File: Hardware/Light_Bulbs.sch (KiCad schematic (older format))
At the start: 44 parts, among them J1 DNP, Q1 2N2222A, Q2 2N2222A, Q3 2N2222A, Q4 2N2222A, U1 PIC18F23K22

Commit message: Replaced light bulb through-hole resistors by SMD ones.
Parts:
- R92, R93, R94, R95: footprint Resistor_THT:R_Axial_DIN0207_L6.3mm_D2.5mm_P7.62mm_Horizontal -> Resistor_SMD:R_1206_3216Metric_Pad1.42x1.75mm_HandSolder
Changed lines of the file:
@@
 EESchema Schematic File Version 4
-LIBS:Chrismas_Tree-cache
 EELAYER 30 0
 EELAYER END
@@
 F 0 "R95" V 1407 5850 50  0000 C CNN
 F 1 "220" V 1316 5850 50  0000 C CNN
-F 2 "Resistor_THT:R_Axial_DIN0207_L6.3mm_D2.5mm_P7.62mm_Horizontal" V 1130 5850 50  0001 C CNN
+F 2 "Resistor_SMD:R_1206_3216Metric_Pad1.42x1.75mm_HandSolder" V 1130 5850 50  0001 C CNN
 F 3 "~" H 1200 5850 50  0001 C CNN
 	1    1200 5850
@@
 F 0 "R94" V 1407 6300 50  0000 C CNN
 F 1 "220" V 1316 6300 50  0000 C CNN
-F 2 "Resistor_THT:R_Axial_DIN0207_L6.3mm_D2.5mm_P7.62mm_Horizontal" V 1130 6300 50  0001 C CNN
+F 2 "Resistor_SMD:R_1206_3216Metric_Pad1.42x1.75mm_HandSolder" V 1130 6300 50  0001 C CNN
 F 3 "~" H 1200 6300 50  0001 C CNN
 	1    1200 6300
@@
 F 0 "R93" V 1407 6750 50  0000 C CNN
 F 1 "220" V 1316 6750 50  0000 C CNN
-F 2 "Resistor_THT:R_Axial_DIN0207_L6.3mm_D2.5mm_P7.62mm_Horizontal" V 1130 6750 50  0001 C CNN
+F 2 "Resistor_SMD:R_1206_3216Metric_Pad1.42x1.75mm_HandSolder" V 1130 6750 50  0001 C CNN
 F 3 "~" H 1200 6750 50  0001 C CNN
 	1    1200 6750
@@
 F 0 "R92" V 1407 7200 50  0000 C CNN
 F 1 "220" V 1316 7200 50  0000 C CNN
-F 2 "Resistor_THT:R_Axial_DIN0207_L6.3mm_D2.5mm_P7.62mm_Horizontal" V 1130 7200 50  0001 C CNN
+F 2 "Resistor_SMD:R_1206_3216Metric_Pad1.42x1.75mm_HandSolder" V 1130 7200 50  0001 C CNN
 F 3 "~" H 1200 7200 50  0001 C CNN
 	1    1200 7200

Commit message: Replaced though-hole capacitors by SMD ones.
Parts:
- C1, C2, C3, C4: footprint Capacitor_THT:C_Disc_D5.0mm_W2.5mm_P5.00mm -> Capacitor_SMD:C_1206_3216Metric_Pad1.42x1.75mm_HandSolder
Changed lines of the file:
@@
 F 0 "C4" H 8865 5646 50  0000 L CNN
 F 1 "100n-25V" H 8865 5555 50  0000 L CNN
-F 2 "Capacitor_THT:C_Disc_D5.0mm_W2.5mm_P5.00mm" H 8788 5450 50  0001 C CNN
+F 2 "Capacitor_SMD:C_1206_3216Metric_Pad1.42x1.75mm_HandSolder" H 8788 5450 50  0001 C CNN
 F 3 "~" H 8750 5600 50  0001 C CNN
 	1    8750 5600
@@
 F 0 "C1" H 4665 2746 50  0000 L CNN
 F 1 "100n-25V" H 4600 2600 50  0000 L CNN
-F 2 "Capacitor_THT:C_Disc_D5.0mm_W2.5mm_P5.00mm" H 4588 2550 50  0001 C CNN
+F 2 "Capacitor_SMD:C_1206_3216Metric_Pad1.42x1.75mm_HandSolder" H 4588 2550 50  0001 C CNN
 F 3 "~" H 4550 2700 50  0001 C CNN
 	1    4550 2700
@@
 F 0 "C2" H 5215 2746 50  0000 L CNN
 F 1 "1u-25V" H 5150 2600 50  0000 L CNN
-F 2 "Capacitor_THT:C_Disc_D5.0mm_W2.5mm_P5.00mm" H 5138 2550 50  0001 C CNN
+F 2 "Capacitor_SMD:C_1206_3216Metric_Pad1.42x1.75mm_HandSolder" H 5138 2550 50  0001 C CNN
 F 3 "~" H 5100 2700 50  0001 C CNN
 	1    5100 2700
@@
 F 0 "C3" H 5715 2746 50  0000 L CNN
 F 1 "10u-25V" H 5650 2600 50  0000 L CNN
-F 2 "Capacitor_THT:C_Disc_D5.0mm_W2.5mm_P5.00mm" H 5638 2550 50  0001 C CNN
+F 2 "Capacitor_SMD:C_1206_3216Metric_Pad1.42x1.75mm_HandSolder" H 5638 2550 50  0001 C CNN
 F 3 "~" H 5600 2700 50  0001 C CNN
 	1    5600 2700

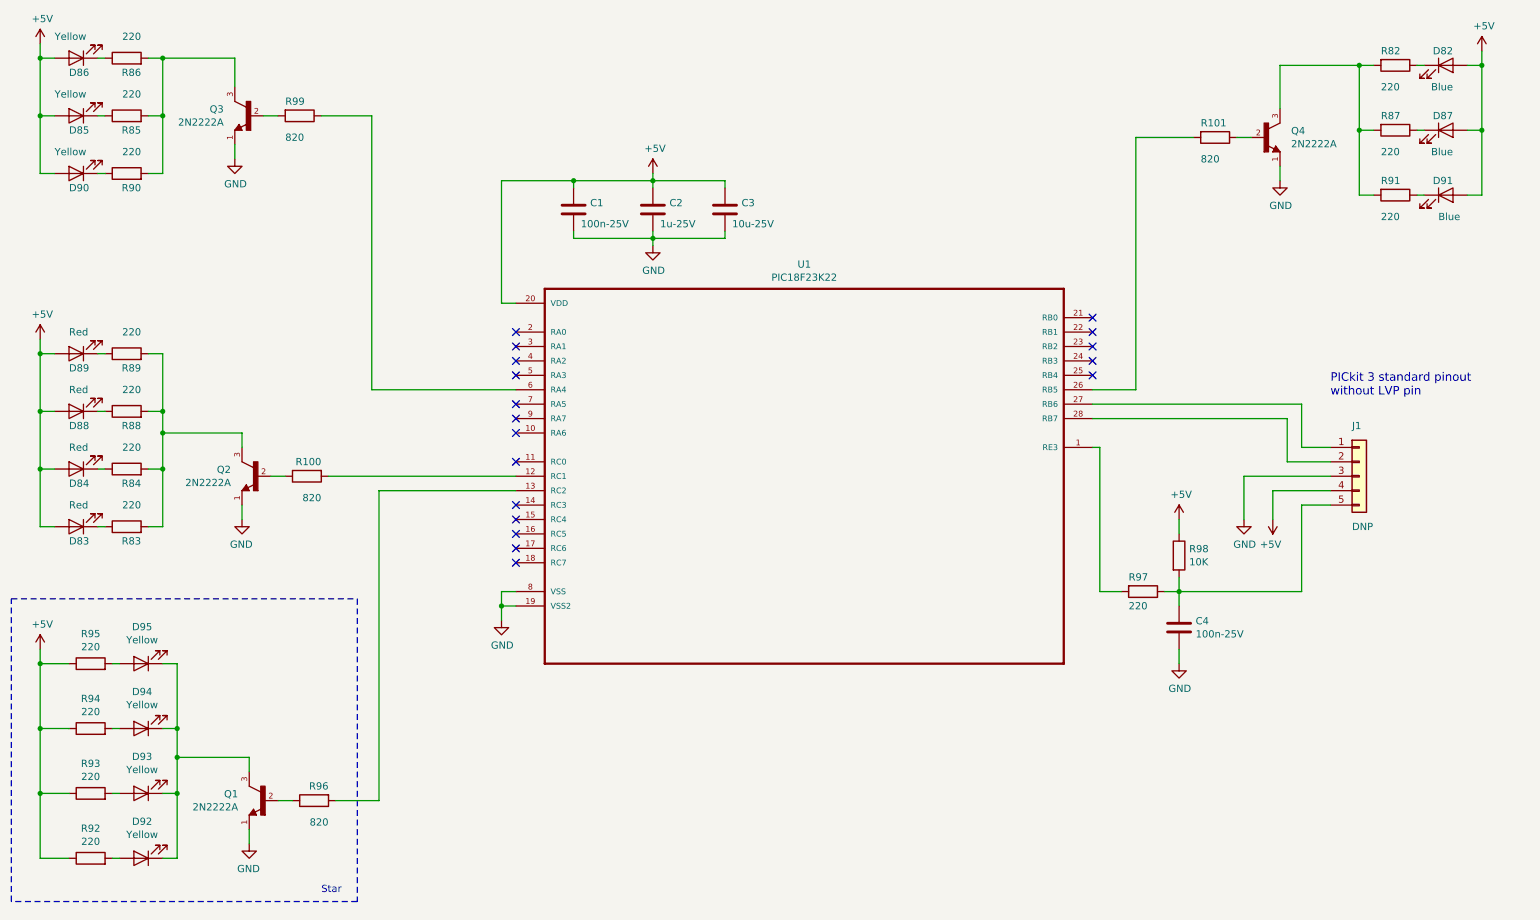
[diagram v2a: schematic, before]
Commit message: Replaced through-hole transistors by SMD ones.
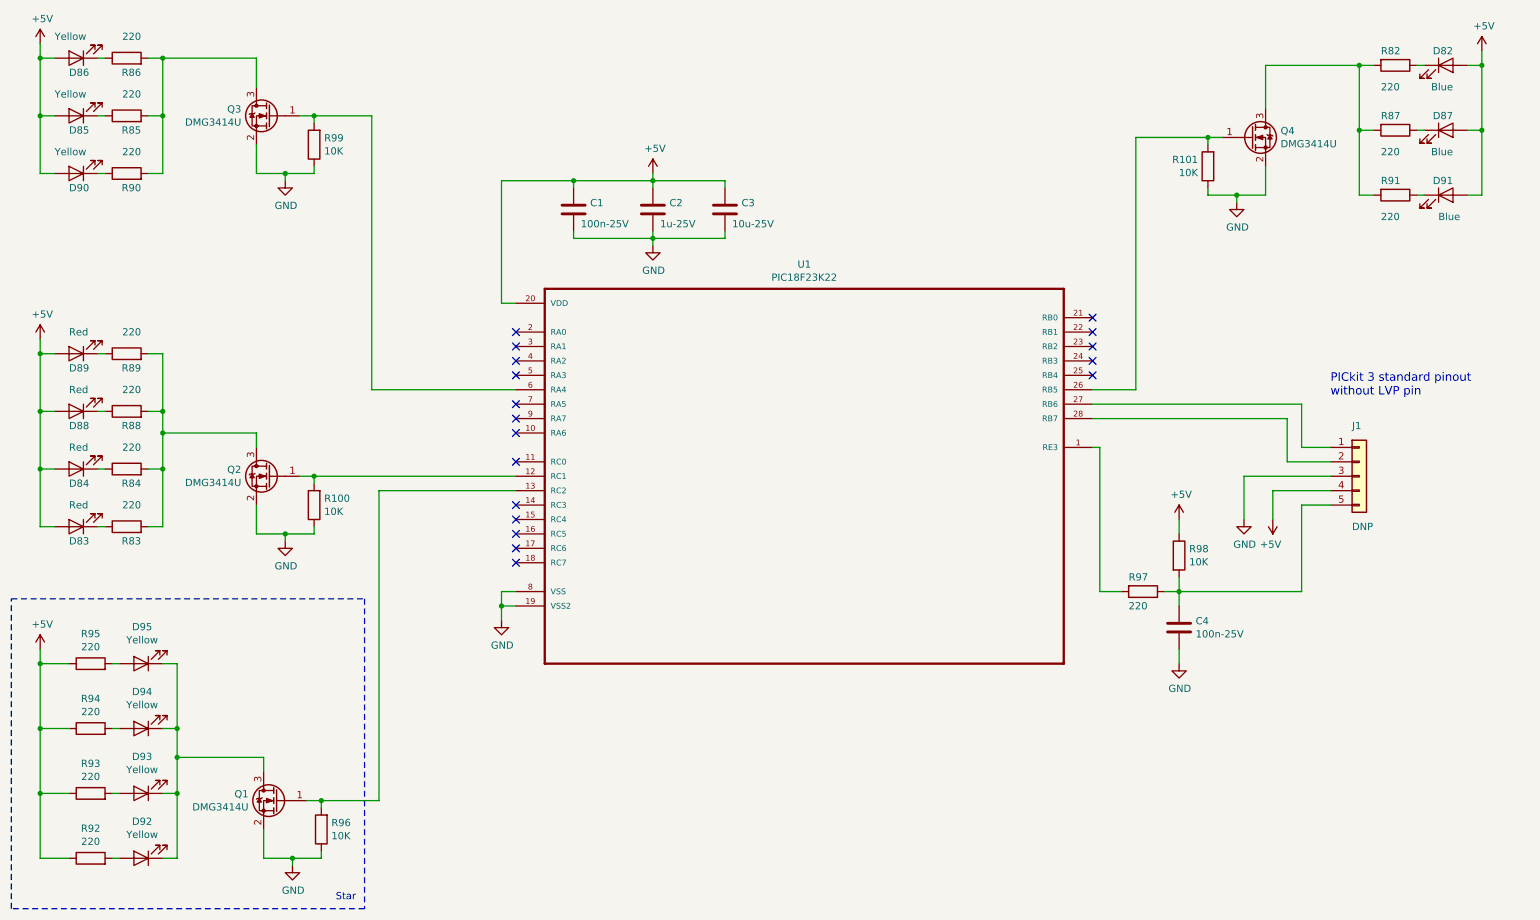
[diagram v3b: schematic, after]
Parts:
- removed Q1, Q2, Q3, Q4: 2N2222A, Package_TO_SOT_THT:TO-18-3, symbol 2N2222A:2N2222A
- added Q1, Q2, Q3, Q4: DMG3414U, Package_TO_SOT_SMD:SOT-23, symbol Transistor_FET:DMG3414U
- R100, R101, R96, R99: value 820 -> 10K; footprint Resistor_THT:R_Axial_DIN0207_L6.3mm_D2.5mm_P7.62mm_Horizontal -> Resistor_SMD:R_1206_3216Metric_Pad1.42x1.75mm_HandSolder
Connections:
- net GND: now also R100.1, R101.1, R96.1, R99.1, Q1.2 (S), Q2.2 (S), Q3.2 (S), Q4.2 (S)
- net at R96.2, U1.13 (RC2): now also Q1.1 (G)
- net at R82.2, R87.2, R91.2: now also Q4.3 (D)
- net at R83.2, R84.2, R88.2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: now also Q2.3 (D)
- net at R85.2, R86.2, R90.2: now also Q3.3 (D)
- net at D92.1 (K), D93.1 (K), D94.1 (K)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: now also Q1.3 (D)
- net at R100.2, U1.12 (RC1): now also Q2.1 (G)
- net at R101.2, U1.26 (RB5): now also Q4.1 (G)
- net at U1.6 (RA4): now also R99.2, Q3.1 (G); no longer R99.1
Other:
- moved on the sheet: R101, R99

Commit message: Changed microcontroller package for a SMD one.
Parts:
- U1: footprint Package_DIP:DIP-28_W7.62mm -> Package_SO:SOIC-28W_7.5x17.9mm_P1.27mm
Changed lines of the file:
@@
 F 0 "U1" H 6150 5820 50  0000 C CNN
 F 1 "PIC18F23K22" H 6150 5729 50  0000 C CNN
-F 2 "Package_DIP:DIP-28_W7.62mm" H 6150 4450 50  0001 C CNN
+F 2 "Package_SO:SOIC-28W_7.5x17.9mm_P1.27mm" H 6150 4450 50  0001 C CNN
 F 3 "" H 6150 4450 50  0001 C CNN
 	1    6150 4450

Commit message: Changed all remaining through-hole resistors by SMD ones in both schematic and PCB.
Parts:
- R82, R83, R84, R85, R86, R87, R88, R89, R90, R91, R97, R98: footprint Resistor_THT:R_Axial_DIN0207_L6.3mm_D2.5mm_P7.62mm_Horizontal -> Resistor_SMD:R_1206_3216Metric_Pad1.30x1.75mm_HandSolder
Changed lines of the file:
@@
 F 0 "R98" H 8820 5146 50  0000 L CNN
 F 1 "10K" H 8820 5055 50  0000 L CNN
-F 2 "Resistor_THT:R_Axial_DIN0207_L6.3mm_D2.5mm_P7.62mm_Horizontal" V 8680 5100 50  0001 C CNN
+F 2 "Resistor_SMD:R_1206_3216Metric_Pad1.30x1.75mm_HandSolder" V 8680 5100 50  0001 C CNN
 F 3 "~" H 8750 5100 50  0001 C CNN
 	1    8750 5100
@@
 F 0 "R97" V 8400 5250 50  0000 L CNN
 F 1 "220" V 8600 5250 50  0000 L CNN
-F 2 "Resistor_THT:R_Axial_DIN0207_L6.3mm_D2.5mm_P7.62mm_Horizontal" V 8430 5350 50  0001 C CNN
+F 2 "Resistor_SMD:R_1206_3216Metric_Pad1.30x1.75mm_HandSolder" V 8430 5350 50  0001 C CNN
 F 3 "~" H 8500 5350 50  0001 C CNN
 	1    8500 5350
@@
 F 0 "R91" V 10150 2500 50  0000 L CNN
 F 1 "220" V 10400 2500 50  0000 L CNN
-F 2 "Resistor_THT:R_Axial_DIN0207_L6.3mm_D2.5mm_P7.62mm_Horizontal" V 10180 2600 50  0001 C CNN
+F 2 "Resistor_SMD:R_1206_3216Metric_Pad1.30x1.75mm_HandSolder" V 10180 2600 50  0001 C CNN
 F 3 "~" H 10250 2600 50  0001 C CNN
 	1    10250 2600
@@
 F 0 "R90" V 1350 2350 50  0000 L CNN
 F 1 "220" V 1600 2350 50  0000 L CNN
-F 2 "Resistor_THT:R_Axial_DIN0207_L6.3mm_D2.5mm_P7.62mm_Horizontal" V 1380 2450 50  0001 C CNN
+F 2 "Resistor_SMD:R_1206_3216Metric_Pad1.30x1.75mm_HandSolder" V 1380 2450 50  0001 C CNN
 F 3 "~" H 1450 2450 50  0001 C CNN
 	1    1450 2450
@@
 F 0 "R89" V 1350 3600 50  0000 L CNN
 F 1 "220" V 1600 3600 50  0000 L CNN
-F 2 "Resistor_THT:R_Axial_DIN0207_L6.3mm_D2.5mm_P7.62mm_Horizontal" V 1380 3700 50  0001 C CNN
+F 2 "Resistor_SMD:R_1206_3216Metric_Pad1.30x1.75mm_HandSolder" V 1380 3700 50  0001 C CNN
 F 3 "~" H 1450 3700 50  0001 C CNN
 	1    1450 3700
@@
 F 0 "R88" V 1350 4000 50  0000 L CNN
 F 1 "220" V 1600 4000 50  0000 L CNN
-F 2 "Resistor_THT:R_Axial_DIN0207_L6.3mm_D2.5mm_P7.62mm_Horizontal" V 1380 4100 50  0001 C CNN
+F 2 "Resistor_SMD:R_1206_3216Metric_Pad1.30x1.75mm_HandSolder" V 1380 4100 50  0001 C CNN
 F 3 "~" H 1450 4100 50  0001 C CNN
 	1    1450 4100
@@
 F 0 "R87" V 10150 2050 50  0000 L CNN
 F 1 "220" V 10400 2050 50  0000 L CNN
-F 2 "Resistor_THT:R_Axial_DIN0207_L6.3mm_D2.5mm_P7.62mm_Horizontal" V 10180 2150 50  0001 C CNN
+F 2 "Resistor_SMD:R_1206_3216Metric_Pad1.30x1.75mm_HandSolder" V 10180 2150 50  0001 C CNN
 F 3 "~" H 10250 2150 50  0001 C CNN
 	1    10250 2150
@@
 F 0 "R86" V 1350 1550 50  0000 L CNN
 F 1 "220" V 1600 1550 50  0000 L CNN
-F 2 "Resistor_THT:R_Axial_DIN0207_L6.3mm_D2.5mm_P7.62mm_Horizontal" V 1380 1650 50  0001 C CNN
+F 2 "Resistor_SMD:R_1206_3216Metric_Pad1.30x1.75mm_HandSolder" V 1380 1650 50  0001 C CNN
 F 3 "~" H 1450 1650 50  0001 C CNN
 	1    1450 1650
@@
 F 0 "R85" V 1350 1950 50  0000 L CNN
 F 1 "220" V 1600 1950 50  0000 L CNN
-F 2 "Resistor_THT:R_Axial_DIN0207_L6.3mm_D2.5mm_P7.62mm_Horizontal" V 1380 2050 50  0001 C CNN
+F 2 "Resistor_SMD:R_1206_3216Metric_Pad1.30x1.75mm_HandSolder" V 1380 2050 50  0001 C CNN
 F 3 "~" H 1450 2050 50  0001 C CNN
 	1    1450 2050
@@
 F 0 "R84" V 1350 4400 50  0000 L CNN
 F 1 "220" V 1600 4400 50  0000 L CNN
-F 2 "Resistor_THT:R_Axial_DIN0207_L6.3mm_D2.5mm_P7.62mm_Horizontal" V 1380 4500 50  0001 C CNN
+F 2 "Resistor_SMD:R_1206_3216Metric_Pad1.30x1.75mm_HandSolder" V 1380 4500 50  0001 C CNN
 F 3 "~" H 1450 4500 50  0001 C CNN
 	1    1450 4500
@@
 F 0 "R83" V 1350 4800 50  0000 L CNN
 F 1 "220" V 1600 4800 50  0000 L CNN
-F 2 "Resistor_THT:R_Axial_DIN0207_L6.3mm_D2.5mm_P7.62mm_Horizontal" V 1380 4900 50  0001 C CNN
+F 2 "Resistor_SMD:R_1206_3216Metric_Pad1.30x1.75mm_HandSolder" V 1380 4900 50  0001 C CNN
 F 3 "~" H 1450 4900 50  0001 C CNN
 	1    1450 4900
@@
 F 0 "R82" V 10150 1600 50  0000 L CNN
 F 1 "220" V 10400 1600 50  0000 L CNN
-F 2 "Resistor_THT:R_Axial_DIN0207_L6.3mm_D2.5mm_P7.62mm_Horizontal" V 10180 1700 50  0001 C CNN
+F 2 "Resistor_SMD:R_1206_3216Metric_Pad1.30x1.75mm_HandSolder" V 10180 1700 50  0001 C CNN
 F 3 "~" H 10250 1700 50  0001 C CNN
 	1    10250 1700

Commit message: Converted all 1206 SMD footprints to KiCad 5.1.10 latest one in both schematic and PCB.
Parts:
- R100, R101, R92, R93, R94, R95, R96, R99: footprint Resistor_SMD:R_1206_3216Metric_Pad1.42x1.75mm_HandSolder -> Resistor_SMD:R_1206_3216Metric_Pad1.30x1.75mm_HandSolder
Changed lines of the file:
@@
 F 0 "R99" H 2680 2204 50  0000 R CNN
 F 1 "10K" H 2680 2295 50  0000 R CNN
-F 2 "Resistor_SMD:R_1206_3216Metric_Pad1.42x1.75mm_HandSolder" V 2680 2250 50  0001 C CNN
+F 2 "Resistor_SMD:R_1206_3216Metric_Pad1.30x1.75mm_HandSolder" V 2680 2250 50  0001 C CNN
 F 3 "~" H 2750 2250 50  0001 C CNN
 	1    2750 2250
@@
 F 0 "R101" H 9019 2354 50  0000 L CNN
 F 1 "10K" H 9019 2445 50  0000 L CNN
-F 2 "Resistor_SMD:R_1206_3216Metric_Pad1.42x1.75mm_HandSolder" V 8880 2400 50  0001 C CNN
+F 2 "Resistor_SMD:R_1206_3216Metric_Pad1.30x1.75mm_HandSolder" V 8880 2400 50  0001 C CNN
 F 3 "~" H 8950 2400 50  0001 C CNN
 	1    8950 2400
@@
 F 0 "R95" V 1407 5850 50  0000 C CNN
 F 1 "220" V 1316 5850 50  0000 C CNN
-F 2 "Resistor_SMD:R_1206_3216Metric_Pad1.42x1.75mm_HandSolder" V 1130 5850 50  0001 C CNN
+F 2 "Resistor_SMD:R_1206_3216Metric_Pad1.30x1.75mm_HandSolder" V 1130 5850 50  0001 C CNN
 F 3 "~" H 1200 5850 50  0001 C CNN
 	1    1200 5850
@@
 F 0 "R94" V 1407 6300 50  0000 C CNN
 F 1 "220" V 1316 6300 50  0000 C CNN
-F 2 "Resistor_SMD:R_1206_3216Metric_Pad1.42x1.75mm_HandSolder" V 1130 6300 50  0001 C CNN
+F 2 "Resistor_SMD:R_1206_3216Metric_Pad1.30x1.75mm_HandSolder" V 1130 6300 50  0001 C CNN
 F 3 "~" H 1200 6300 50  0001 C CNN
 	1    1200 6300
@@
 F 0 "R93" V 1407 6750 50  0000 C CNN
 F 1 "220" V 1316 6750 50  0000 C CNN
-F 2 "Resistor_SMD:R_1206_3216Metric_Pad1.42x1.75mm_HandSolder" V 1130 6750 50  0001 C CNN
+F 2 "Resistor_SMD:R_1206_3216Metric_Pad1.30x1.75mm_HandSolder" V 1130 6750 50  0001 C CNN
 F 3 "~" H 1200 6750 50  0001 C CNN
 	1    1200 6750
@@
 F 0 "R92" V 1407 7200 50  0000 C CNN
 F 1 "220" V 1316 7200 50  0000 C CNN
-F 2 "Resistor_SMD:R_1206_3216Metric_Pad1.42x1.75mm_HandSolder" V 1130 7200 50  0001 C CNN
+F 2 "Resistor_SMD:R_1206_3216Metric_Pad1.30x1.75mm_HandSolder" V 1130 7200 50  0001 C CNN
 F 3 "~" H 1200 7200 50  0001 C CNN
 	1    1200 7200
@@
 F 0 "R100" H 2680 4704 50  0000 R CNN
 F 1 "10K" H 2680 4795 50  0000 R CNN
-F 2 "Resistor_SMD:R_1206_3216Metric_Pad1.42x1.75mm_HandSolder" V 2680 4750 50  0001 C CNN
+F 2 "Resistor_SMD:R_1206_3216Metric_Pad1.30x1.75mm_HandSolder" V 2680 4750 50  0001 C CNN
 F 3 "~" H 2750 4750 50  0001 C CNN
 	1    2750 4750
@@
 F 0 "R96" H 2730 6954 50  0000 R CNN
 F 1 "10K" H 2730 7045 50  0000 R CNN
-F 2 "Resistor_SMD:R_1206_3216Metric_Pad1.42x1.75mm_HandSolder" V 2730 7000 50  0001 C CNN
+F 2 "Resistor_SMD:R_1206_3216Metric_Pad1.30x1.75mm_HandSolder" V 2730 7000 50  0001 C CNN
 F 3 "~" H 2800 7000 50  0001 C CNN
 	1    2800 7000
